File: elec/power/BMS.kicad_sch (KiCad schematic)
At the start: 37 parts, among them J1 Conn_01x05_Socket, J2 Conn_01x02_Socket, Q1 NMOS, Q2 NMOS, U1 BQ7791501PWR

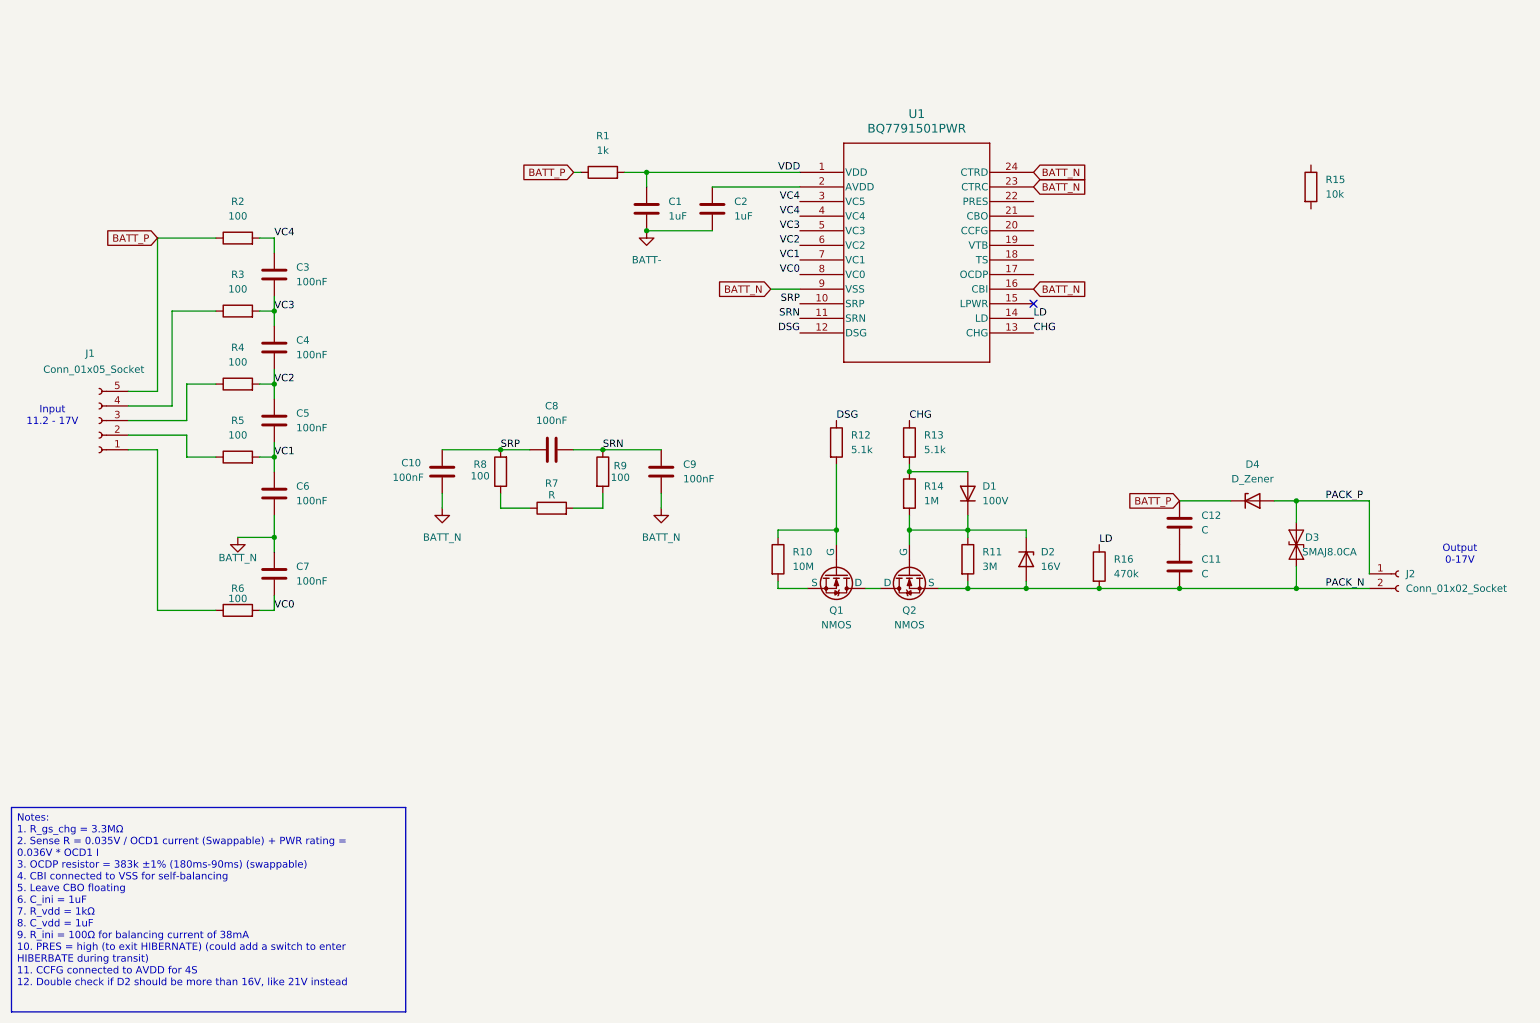
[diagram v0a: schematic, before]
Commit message: BMS schematic almost done + components are assigned their footpritns except connectors
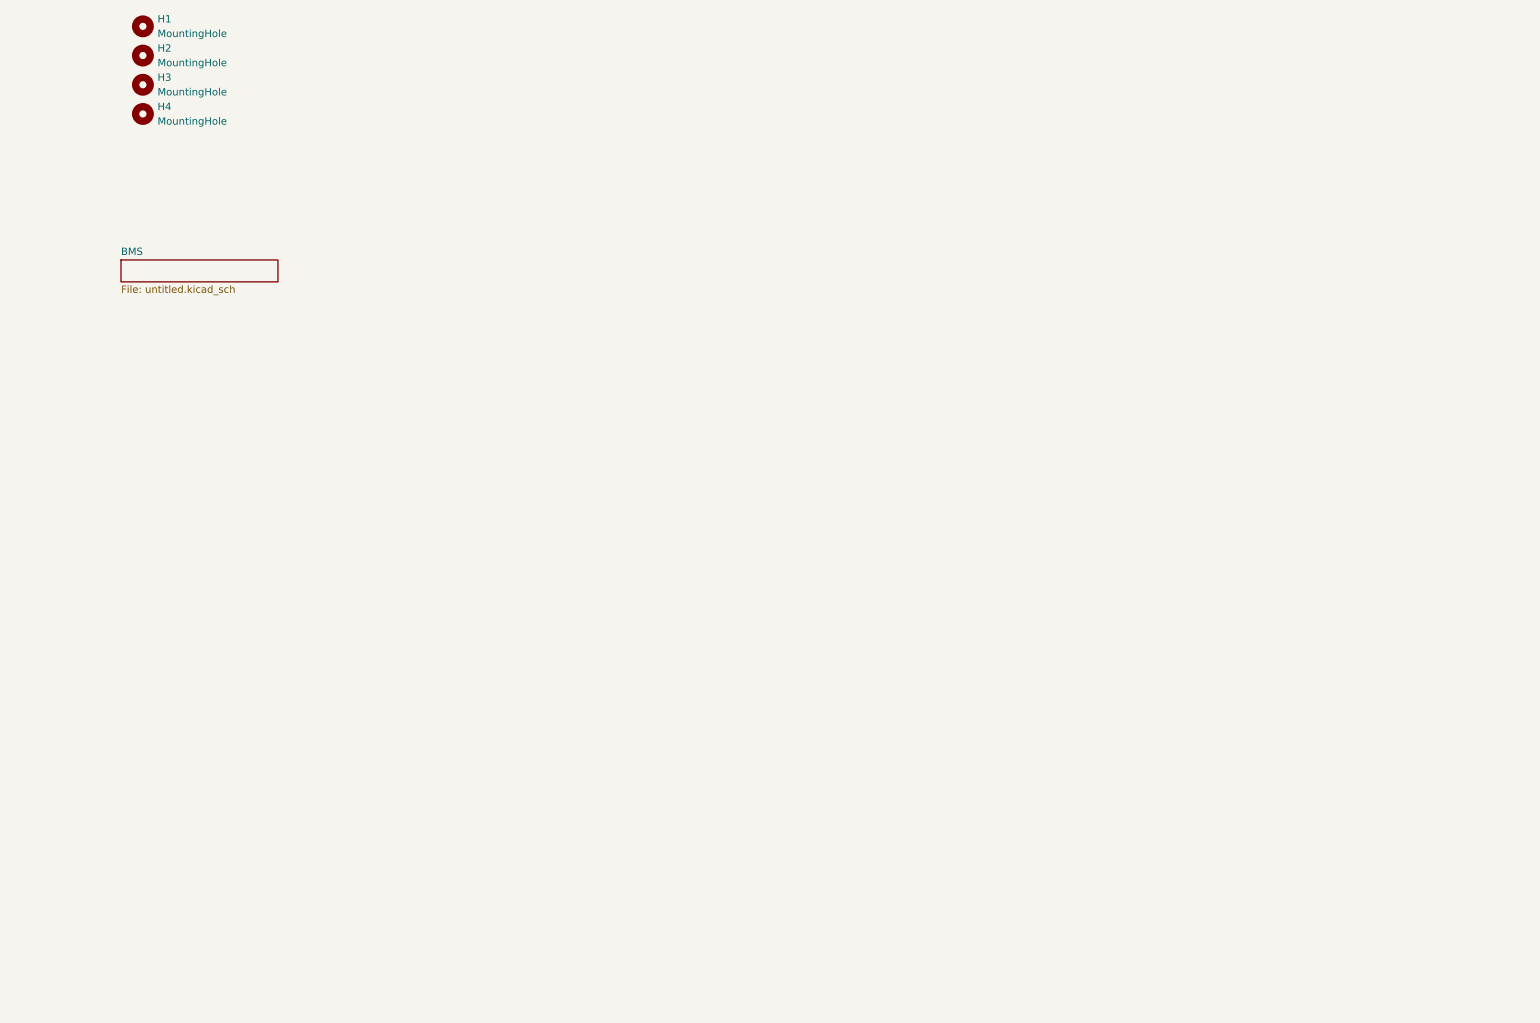
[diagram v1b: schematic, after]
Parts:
- removed C1, C2: 1uF, symbol Device:C
- removed C10, C3, C4, C5, C6, C7, C8, C9: 100nF, symbol Device:C
- removed C11, C12: C, symbol Device:C
- removed D1: 100V, symbol Device:D
- removed D2: 16V, symbol Device:D_Zener
- removed D3: SMAJ8.0CA, Diode_SMD:D_SMA, symbol Diode:SMAJ8.0CA
- removed D4: D_Zener, symbol Device:D_Zener
- removed J1: Conn_01x05_Socket, symbol Connector:Conn_01x05_Socket
- removed J2: Conn_01x02_Socket, symbol Connector:Conn_01x02_Socket
- removed Q1, Q2: NMOS, symbol Simulation_SPICE:NMOS
- removed R1: 1k, symbol Device:R
- removed R10: 10M, symbol Device:R
- removed R11: 3M, symbol Device:R
- removed R12, R13: 5.1k, symbol Device:R
- removed R14: 1M, symbol Device:R
- removed R15: 10k, symbol Device:R
- removed R16: 470k, symbol Device:R
- removed R2, R3, R4, R5, R6, R8, R9: 100, symbol Device:R
- removed R7: R, symbol Device:R
- removed U1: BQ7791501PWR, TSSOP24_PW_TEX, symbol 2026-04-14_23-08-16:BQ7791501PWR
- added H1, H2, H3, H4: MountingHole, MountingHole:MountingHole_3.2mm_M3, symbol Mechanical:MountingHole
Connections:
- no-connect marks 1 -> 0
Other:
- added sheet BMS (untitled.kicad_sch)
- note removed: "Input 11.2 - 17V"
- note removed: "Output 0-17V"

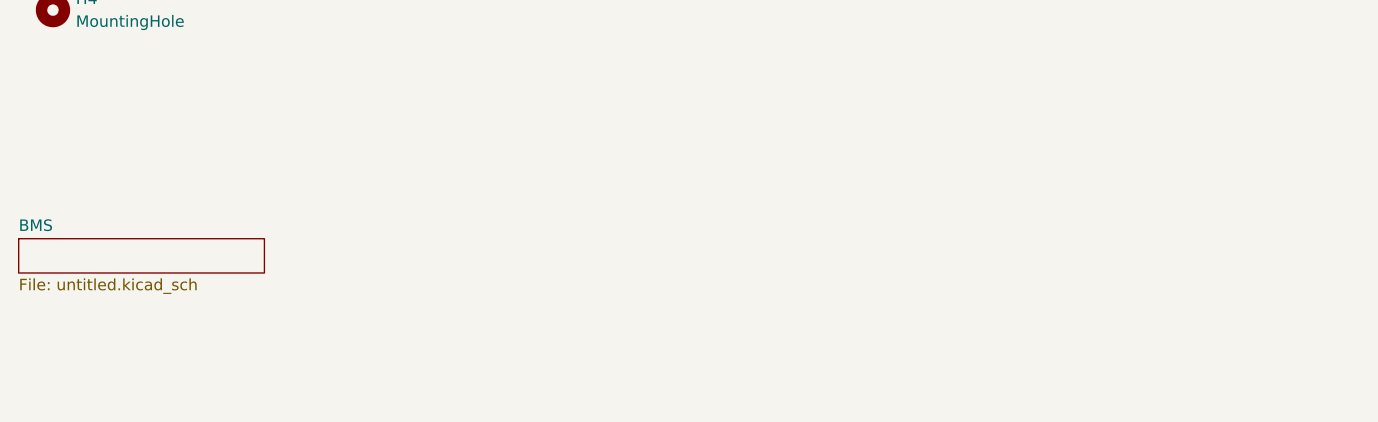
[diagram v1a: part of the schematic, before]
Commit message: Add fuel gauge schematic
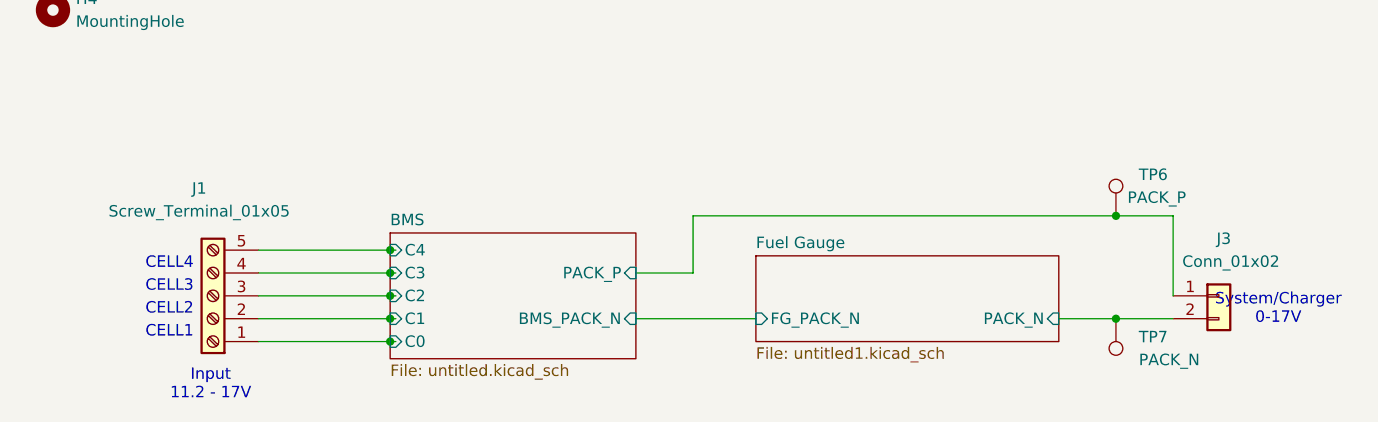
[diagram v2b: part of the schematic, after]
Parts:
- added J1: Screw_Terminal_01x05, symbol Connector:Screw_Terminal_01x05
- added J3: Conn_01x02, symbol Connector_Generic:Conn_01x02
- added TP6: PACK_P, TestPoint:TestPoint_Pad_D2.0mm, symbol Connector:TestPoint
- added TP7: PACK_N, TestPoint:TestPoint_Pad_D2.0mm, symbol Connector:TestPoint
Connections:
- new net BMS/C0: J1.1 (Pin_1)
- new net BMS/C1: J1.2 (Pin_2)
- new net BMS/C2: J1.3 (Pin_3)
- new net BMS/C3: J1.4 (Pin_4)
- new net BMS/C4: J1.5 (Pin_5)
- new net BMS/PACK_P: J3.1 (Pin_1), TP6.1
- new net Fuel Gauge/PACK_N: J3.2 (Pin_2), TP7.1
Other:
- added sheet Fuel Gauge (untitled1.kicad_sch)
- sheet BMS ports: added BMS_PACK_N, C0, C1, C2, C3, C4, PACK_P; removed none
- note added: "CELL1"
- note added: "CELL2"
- note added: "CELL3"
- note added: "CELL4"
- note added: "Input 11.2 - 17V"
- note added: "System/Charger 0-17V"
